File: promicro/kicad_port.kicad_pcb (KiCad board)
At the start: 2 copper layers, 100 x 86 mm, 19 parts, among them J1 Conn_01x13, J2 Conn_01x13, J3 Conn_01x13, J4 Conn_01x13, J5 Conn_01x10, J6 Conn_01x10, M1 MountingHole_6.4mm_M6, M3 MountingHole_4.3mm_M4, M4 MountingHole_4.3mm_M4, U1 Elite-C

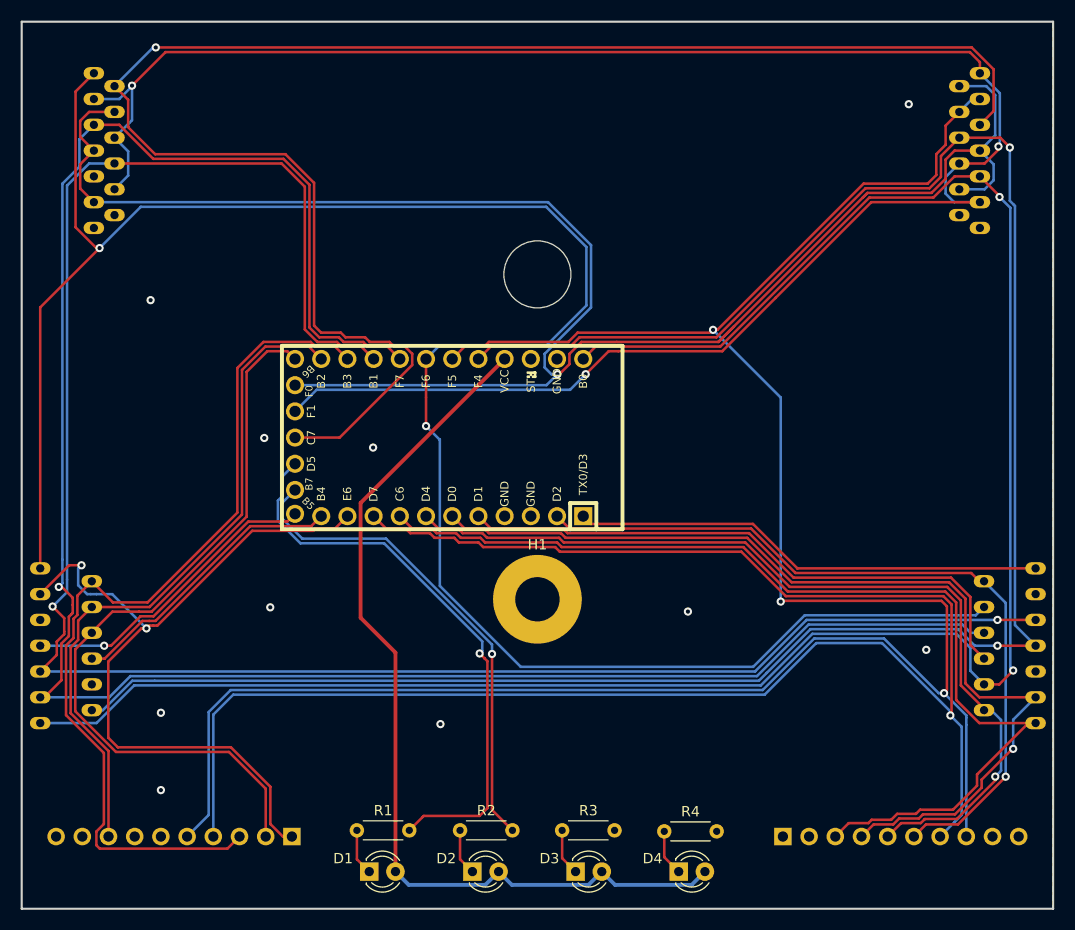
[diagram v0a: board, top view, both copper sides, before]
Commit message: Add Advantage compatibility
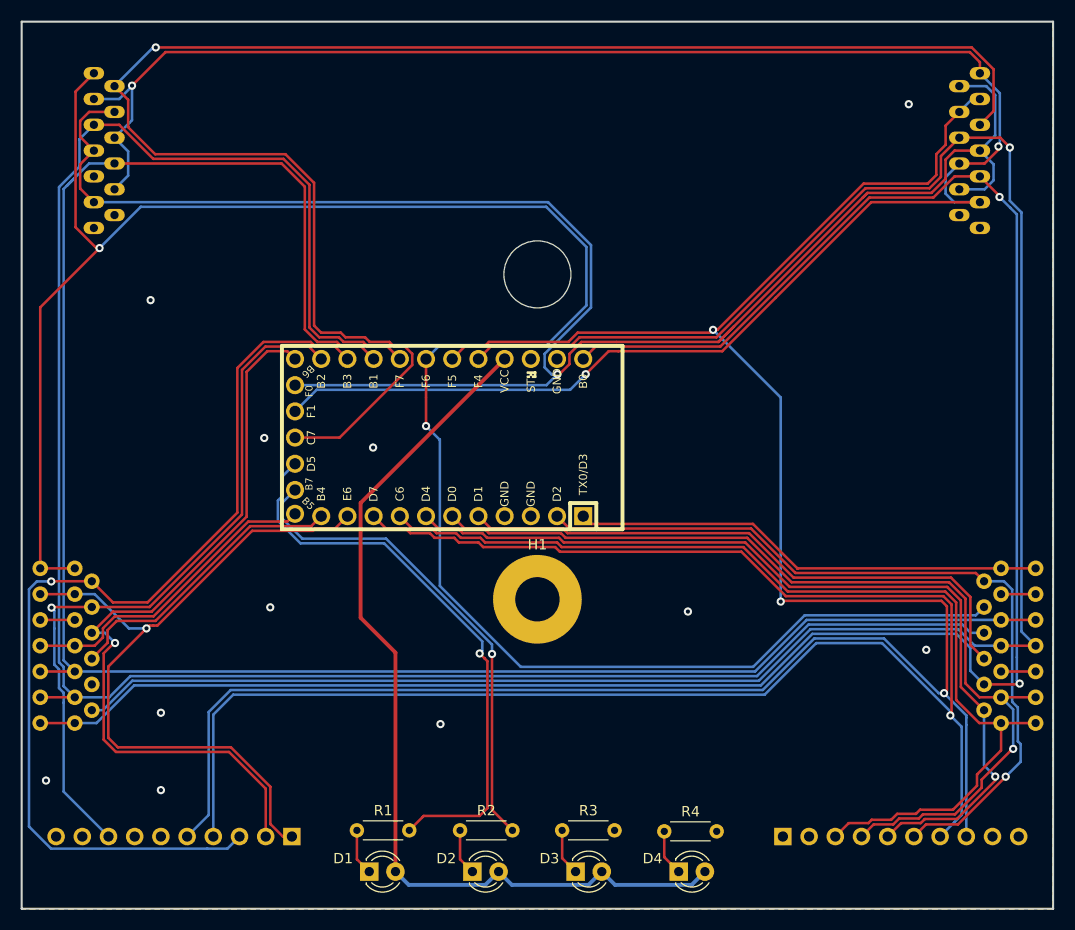
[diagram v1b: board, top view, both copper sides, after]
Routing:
- net /ROW_5: track 87.9 -> 96.2 mm, vias 0 -> 1
- net /ROW_4: track 75.9 -> 71.7 mm, vias 2 -> 1
- net /ROW_3: track 66.0 -> 69.8 mm, vias 0 -> 1
- net /COL_0: track 207.1 -> 210.4 mm
- net unconnected-(J3-Pad9): track 0.00 -> 3.35 mm
- net unconnected-(J3-Pad3): track 0.00 -> 3.35 mm
- net unconnected-(J4-Pad9): track 0.00 -> 3.35 mm
- net /ROW_9: track 75.1 -> 77.5 mm
- net /ROW_6: track 100.1 -> 98.3 mm
- net /COL_2: track 201.1 -> 199.5 mm, vias 1 -> 0
- net /COL_4: track 196.8 -> 198.5 mm
- net /ROW_8: track 87.6 -> 86.7 mm
- net /ROW_EQL: track 28.0 -> 28.7 mm
- net /ROW_1: track 30.0 -> 30.5 mm, vias 1 -> 0
- net /ROW_2: track 74.1 -> 74.4 mm, vias 0 -> 1
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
